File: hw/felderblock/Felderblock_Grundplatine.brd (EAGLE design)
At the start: 100 x 80 mm, 47 parts, among them IC1 LM311N, IC2 LM2936Z-5.0, J1 RJ11, J2 RJ11, M1 ARDUINO-NANO-3.0, T1 BC337, X1 TASTENSPERRE1, X2 TASTENSPERRE2, X3 SCHLUESSELSPERRE, X4 I2C

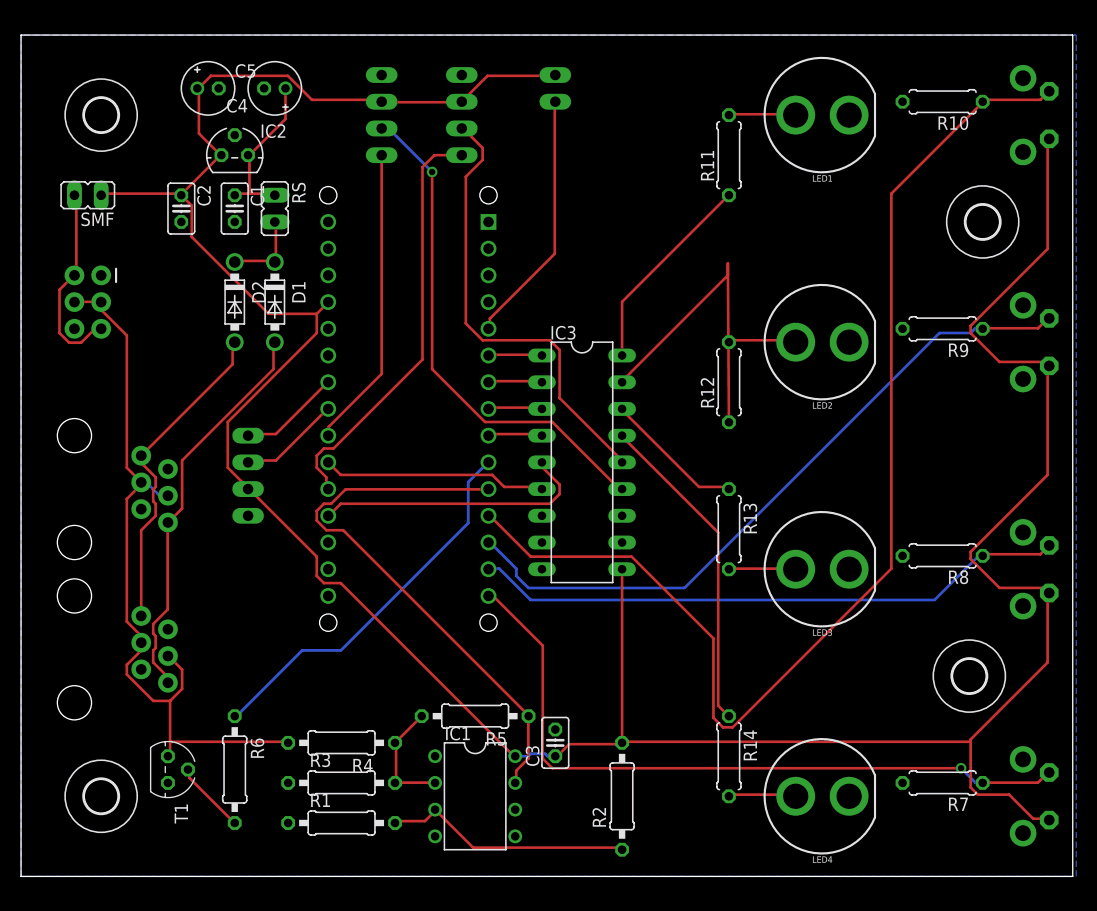
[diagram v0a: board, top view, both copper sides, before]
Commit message: MI+AsT integrated
LED nach I2C, MI links und rechts, AsT und AsM integriert. Board rerouted
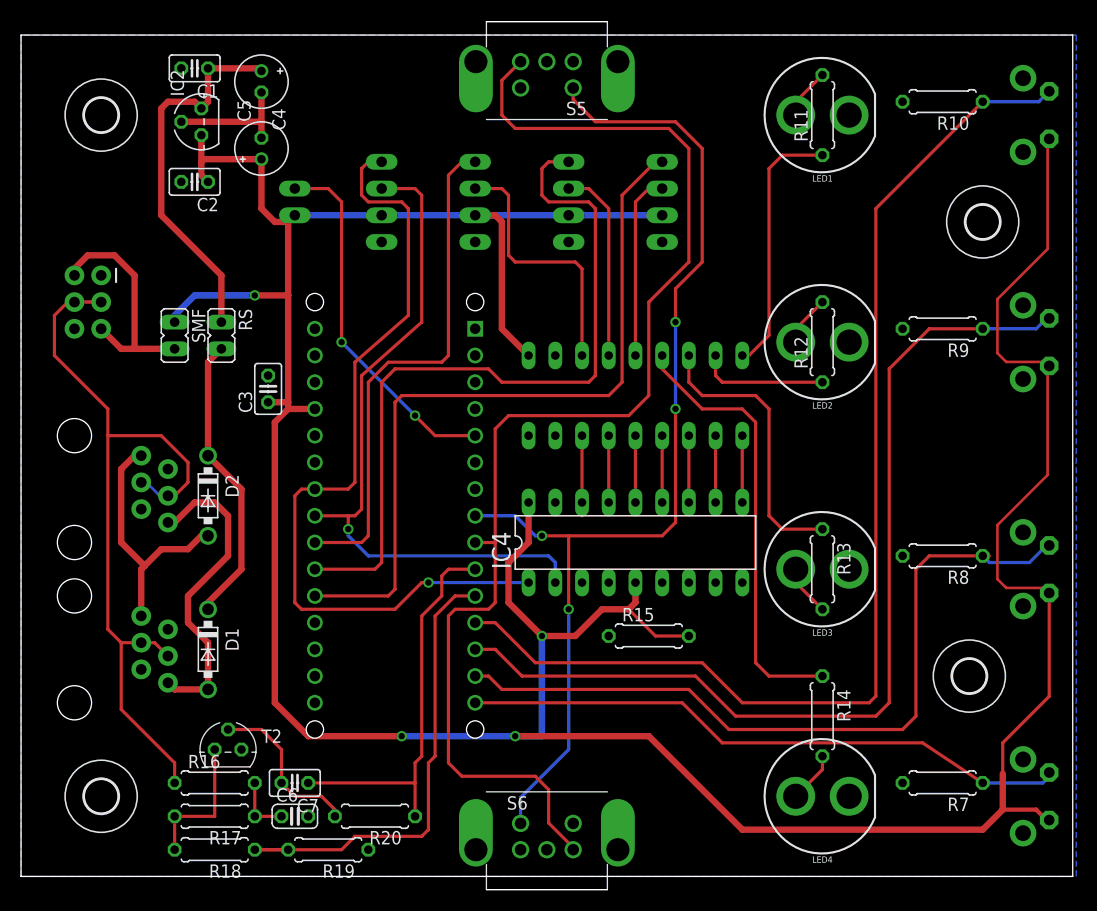
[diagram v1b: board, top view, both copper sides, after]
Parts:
- removed IC1: LM311N, linear:DIL08
- removed R1: 22k, resistor:0207/10
- removed R2: 10k, resistor:0207/10
- removed R3: 150k, resistor:0207/10
- removed R4: 47k, resistor:0207/10
- removed R5: 220k, resistor:0207/10
- removed R6: 2.2k, resistor:0207/10
- removed T1: BC337, transistor:TO92
- added C6: 47pF, resistor:C025-024X044
- added C7: 1nF, resistor:C025-025X050
- added IC4: MCP2300X/P, adafruit:DIL18
- added R15: 1k, resistor:0207/7
- added R16, R17: 12R, resistor:0207/7
- added R18: 130K, resistor:0207/7
- added R19: 47k, resistor:0207/7
- added R20: 3K3, resistor:0207/7
- added S5, S6: EC11B42AE, alps:EC11B42
- added T2: BC337, transistor:TO92
- added X5: ANSCHALTER, con-molex:22-23-2041
- moved C3 43.3 mm to (23.5, 46.4)
- moved D1 33.6 mm to (17.8, 21.6)
- moved X4 29.0 mm to (34.3, 64.1)
- moved X3 27.0 mm to (26.0, 64.1), turned to 90 degrees
- moved X1 20.8 mm to (61.0, 64.1), turned to 90 degrees
- moved X2 19.6 mm to (52.1, 64.1), turned to 90 degrees
- moved D2 18.6 mm to (17.8, 36.2)
- moved SMF 15.7 mm to (14.6, 51.4), turned to 180 degrees
- moved C1 13.9 mm to (16.5, 76.8), turned to 180 degrees
- moved RS 13.1 mm to (19.1, 51.4)
- moved M1 10.2 mm to (35.6, 34.3)
- moved R11 9.67 mm to (76.2, 72.4)
- moved R13 9.67 mm to (76.2, 29.2)
- moved R14 9.67 mm to (76.2, 15.2)
- moved R12 9.67 mm to (76.2, 50.8)
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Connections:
- removed net GND.2: M1.J2.2
- removed net N$1: IC1.3, R1.2, R2.1
- removed net N$18: IC3.7
- removed net N$2: R6.2, T1.2
- removed net N$26: IC3.12
- removed net N$3: IC1.2, R3.2, R4.1, R5.2
- new net AS_LED: IC3.7, IC4.16
- new net AS_LEDD: IC3.12, X5.3
- new net AS_SW: M1.J2.9, X5.4
- new net BASE: C7.2, R20.2, T2.2
- new net LN_INTERN: R17.2, R18.2, T2.3
- new net MI_FWD: M1.J1.9, S5.B, S6.B
- new net MI_SW: M1.J1.8, S5.D, S6.D
- new net N$11: C6.1, R16.2, R17.1
- net +5V: now also IC4.18, IC4.5, R15.2, X5.2; no longer IC1.8, R2.2
- net FELD1_LED: now also IC4.10; no longer M1.J1.6
- net FELD2_LED: now also IC4.11; no longer M1.J1.7
- net FELD3_LED: now also IC4.12; no longer M1.J1.8
- net FELD4_LED: now also IC4.13; no longer M1.J1.9
- net GND: now also C6.2, IC4.3, IC4.4, IC4.6, IC4.8, IC4.9, M1.J2.2, R15.1, R19.1, S5.C, S5.E, S5.GND1, S5.GND2, S6.C, S6.E, S6.GND1, S6.GND2, T2.1, X5.1; no longer IC1.1, IC1.4, R1.1, R3.1, T1.1
- net LN_RX: now also R18.1, R19.2; no longer IC1.7, R5.1
- net LN_TX: now also C7.1, R20.1; no longer R6.1
- net LOCONET: now also R16.1; no longer R4.2, T1.3
- net SCL: now also IC4.1
- net SDA: now also IC4.2
- net TSP1_LED: now also IC4.14; no longer M1.J2.12
- net TSP2_LED: now also IC4.15; no longer M1.J2.10
- net TSP2_SW: now also M1.J2.10; no longer M1.J2.9
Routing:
- net MI_FWD: track 0.00 -> 120.5 mm
- net MI_SW: track 0.00 -> 101.5 mm, vias 0 -> 4
- net SCL: track 9.72 -> 78.0 mm, vias 0 -> 1
- net SDA: track 9.73 -> 65.7 mm, vias 0 -> 1
- net +5V: track 287.5 -> 337.2 mm, vias 0 -> 4
- net AS_SW: track 0.00 -> 48.8 mm
- net TSP2_SW: track 28.8 -> 72.2 mm
- net TSP1_SW: track 40.0 -> 70.9 mm
- net TSP2_LEDD: track 48.2 -> 18.6 mm, vias 1 -> 0
- net TSP1_LEDD: track 43.2 -> 17.7 mm
- net FELD2_SW: track 66.2 -> 91.5 mm
- net AS_LEDD: track 0.00 -> 24.9 mm
- net N$1: track 23.9 -> 0.00 mm
- net N$7: track 15.6 -> 36.3 mm
- net TSP1_LED: track 26.6 -> 6.35 mm
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
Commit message: Update Felderblock_Grundplatine.brd
Mirror MI
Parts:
- flipped S5 to the bottom
- flipped S6 to the bottom
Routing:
- net MI_SW: track 101.5 -> 104.8 mm
- net N$10: vias 0 -> 2
- net LOCONET: vias 0 -> 3
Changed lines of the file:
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@@
 <attribute name="OC_FARNELL" value="1462920" x="34.29" y="64.135" size="1.778" layer="28" rot="MR90" display="off"/>
 </element>
-<element name="S5" library="alps" package="EC11B42" value="EC11B42AE" x="50" y="77.47" rot="R180"/>
-<element name="S6" library="alps" package="EC11B42" value="EC11B42AE" x="50" y="2.54"/>
+<element name="S5" library="alps" package="EC11B42" value="EC11B42AE" x="50" y="77.47" rot="MR180"/>
+<element name="S6" library="alps" package="EC11B42" value="EC11B42AE" x="50" y="2.54" rot="MR0"/>
 <element name="IC4" library="adafruit" package="DIL18" value="MCP2300X/P" x="58.42" y="31.75"/>
 <element name="R15" library="resistor" package="0207/7" value="1k" x="59.69" y="22.86"/>
@@
 <wire x1="9.525" y1="15.875" x2="14.605" y2="10.795" width="0.3048" layer="1"/>
 <wire x1="14.605" y1="10.795" x2="14.605" y2="8.89" width="0.3048" layer="1"/>
+<via x="5.2578" y="54.6354" extent="1-16" drill="0.6" shape="square"/>
+<via x="7.5438" y="54.6354" extent="1-16" drill="0.6" shape="square"/>
+<via x="4.445" y="54.61" extent="1-16" drill="0.6" shape="square"/>
 </signal>
 <signal name="LN_RX">
@@
 <wire x1="8.89" y1="59.055" x2="10.795" y2="57.15" width="0.6096" layer="1"/>
 <wire x1="10.795" y1="57.15" x2="10.795" y2="50.165" width="0.6096" layer="1"/>
+<via x="9.525" y="50.165" extent="1-16" drill="0.6" shape="square"/>
+<via x="5.08" y="57.785" extent="1-16" drill="0.6" shape="square"/>
 </signal>
 <signal name="TSP1_SW">
@@
 <contactref element="S6" pad="B"/>
 <contactref element="M1" pad="J1.9"/>
-<wire x1="52.5" y1="2.54" x2="52.5" y2="2.745" width="0.3048" layer="1"/>
-<wire x1="52.5" y1="2.745" x2="50.165" y2="5.08" width="0.3048" layer="1"/>
-<wire x1="50.165" y1="5.08" x2="50.165" y2="8.255" width="0.3048" layer="1"/>
-<wire x1="50.165" y1="8.255" x2="48.895" y2="9.525" width="0.3048" layer="1"/>
-<wire x1="48.895" y1="9.525" x2="41.91" y2="9.525" width="0.3048" layer="1"/>
 <wire x1="41.91" y1="9.525" x2="40.64" y2="10.795" width="0.3048" layer="1"/>
 <wire x1="40.64" y1="10.795" x2="40.64" y2="24.765" width="0.3048" layer="1"/>
@@
 <wire x1="63.5" y1="58.42" x2="63.5" y2="69.215" width="0.3048" layer="1"/>
 <wire x1="63.5" y1="69.215" x2="61.595" y2="71.12" width="0.3048" layer="1"/>
-<wire x1="61.595" y1="71.12" x2="46.99" y2="71.12" width="0.3048" layer="1"/>
-<wire x1="46.99" y1="71.12" x2="45.72" y2="72.39" width="0.3048" layer="1"/>
-<wire x1="45.72" y1="72.39" x2="45.72" y2="75.69" width="0.3048" layer="1"/>
-<wire x1="45.72" y1="75.69" x2="47.5" y2="77.47" width="0.3048" layer="1"/>
 <wire x1="43.18" y1="31.75" x2="45.085" y2="31.75" width="0.3048" layer="1"/>
+<wire x1="52.5" y1="77.47" x2="52.07" y2="77.47" width="0.254" layer="1"/>
+<wire x1="52.07" y1="77.47" x2="50.8" y2="76.2" width="0.254" layer="1"/>
+<wire x1="50.8" y1="76.2" x2="46.355" y2="76.2" width="0.254" layer="1"/>
+<wire x1="46.355" y1="76.2" x2="45.72" y2="75.565" width="0.254" layer="1"/>
+<wire x1="45.72" y1="75.565" x2="45.72" y2="72.39" width="0.254" layer="1"/>
+<wire x1="45.72" y1="72.39" x2="46.99" y2="71.12" width="0.254" layer="1"/>
+<wire x1="46.99" y1="71.12" x2="61.595" y2="71.12" width="0.254" layer="1"/>
+<wire x1="41.91" y1="9.525" x2="43.18" y2="9.525" width="0.3048" layer="1"/>
+<wire x1="43.18" y1="9.525" x2="45.72" y2="6.985" width="0.3048" layer="1"/>
+<wire x1="45.72" y1="6.985" x2="45.72" y2="3.175" width="0.3048" layer="1"/>
+<wire x1="45.72" y1="3.175" x2="46.355" y2="2.54" width="0.3048" layer="1"/>
+<wire x1="46.355" y1="2.54" x2="47.5" y2="2.54" width="0.3048" layer="1"/>
 </signal>
 <signal name="AS_LED">
@@
 <contactref element="S6" pad="D"/>
 <contactref element="S5" pad="D"/>
-<wire x1="52.5" y1="74.97" x2="52.5" y2="73.865" width="0.3048" layer="1"/>
-<wire x1="52.5" y1="73.865" x2="54.61" y2="71.755" width="0.3048" layer="1"/>
 <wire x1="54.61" y1="71.755" x2="62.23" y2="71.755" width="0.3048" layer="1"/>
 <wire x1="62.23" y1="71.755" x2="64.77" y2="69.215" width="0.3048" layer="1"/>
@@
 <wire x1="48.895" y1="32.385" x2="46.99" y2="34.29" width="0.3048" layer="16"/>
 <wire x1="46.99" y1="34.29" x2="43.18" y2="34.29" width="0.3048" layer="16"/>
-<wire x1="47.5" y1="5.04" x2="47.5" y2="7.495" width="0.3048" layer="16"/>
-<wire x1="47.5" y1="7.495" x2="52.07" y2="12.065" width="0.3048" layer="16"/>
-<wire x1="52.07" y1="12.065" x2="52.07" y2="25.4" width="0.3048" layer="16"/>
+<wire x1="52.07" y1="5.47" x2="52.07" y2="25.4" width="0.3048" layer="16"/>
 <via x="52.07" y="25.4" extent="1-16" drill="0.6" shape="square"/>
 <wire x1="52.07" y1="25.4" x2="52.07" y2="32.385" width="0.3048" layer="1"/>
+<wire x1="54.61" y1="71.755" x2="49.53" y2="71.755" width="0.254" layer="1"/>
+<wire x1="49.53" y1="71.755" x2="47.625" y2="73.66" width="0.254" layer="1"/>
+<wire x1="47.625" y1="73.66" x2="47.625" y2="74.845" width="0.254" layer="1"/>
+<wire x1="47.625" y1="74.845" x2="47.5" y2="74.97" width="0.254" layer="1"/>
+<wire x1="52.07" y1="5.47" x2="52.5" y2="5.04" width="0.3048" layer="16"/>
 </signal>
 <signal name="TSP2_SW">

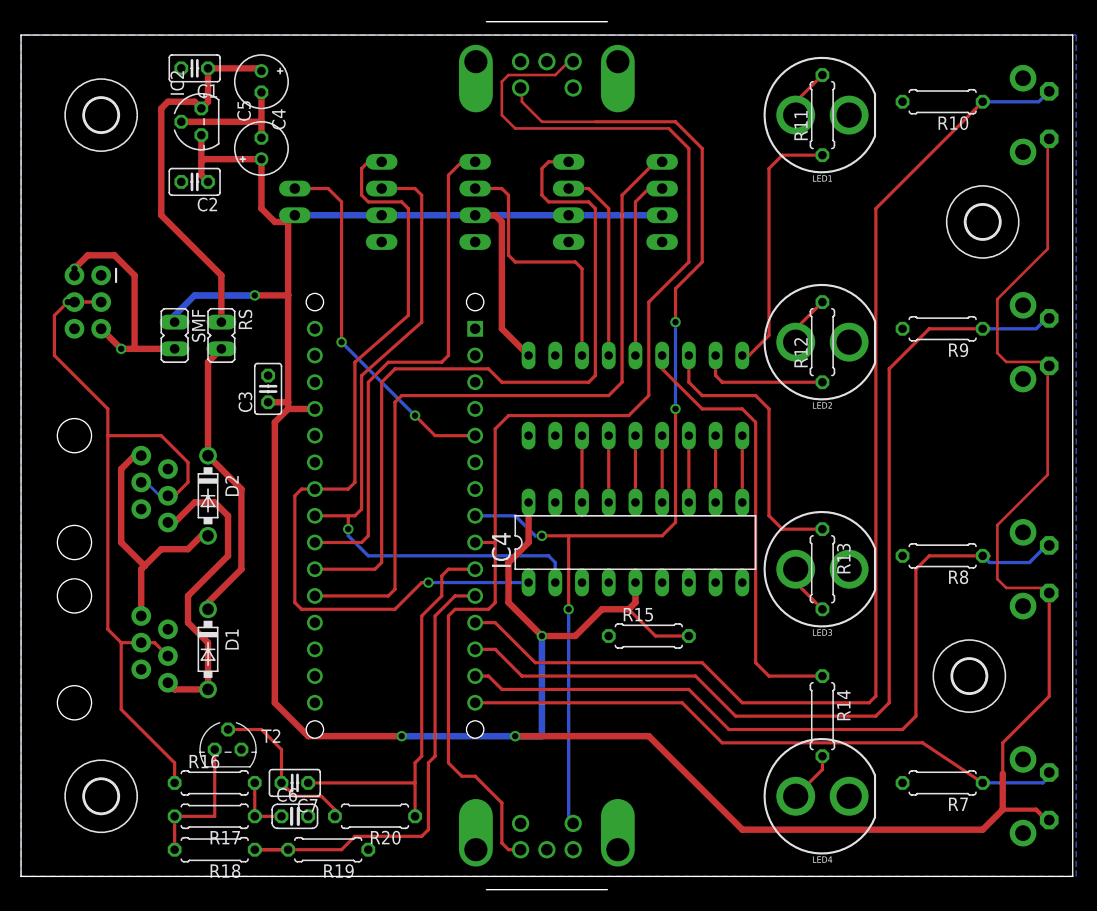
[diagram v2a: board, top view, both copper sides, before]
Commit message: Changed pin order on MCP
MCP moved to other side, changed pin order
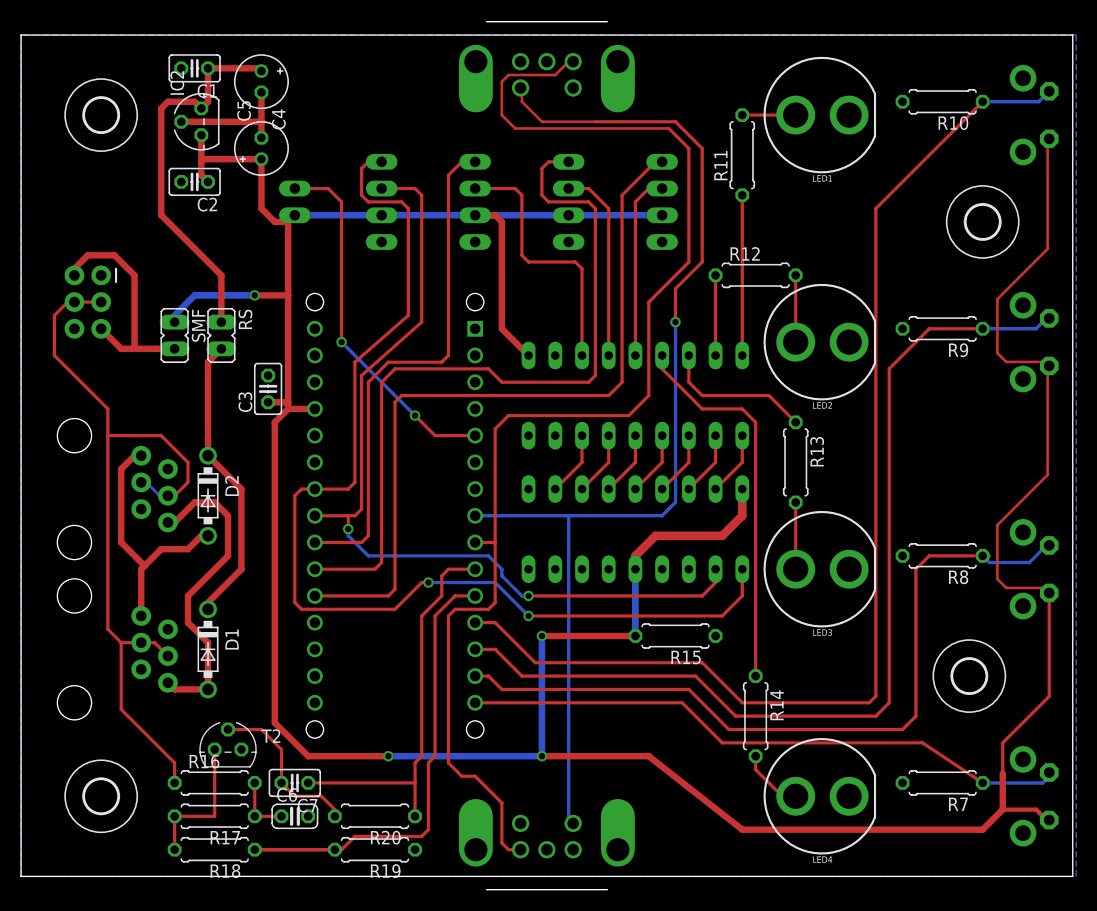
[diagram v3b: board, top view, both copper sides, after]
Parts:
- IC3: value (none) -> ULN2803
- moved R13 10.5 mm to (73.7, 39.4)
- moved R12 8.98 mm to (69.8, 57.1), turned to 0 degrees
- moved R11 8.52 mm to (68.6, 68.6)
- moved R14 6.35 mm to (69.8, 15.2)
- moved R19 4.45 mm to (33.7, 2.54)
- moved R15 2.54 mm to (62.2, 22.9), turned to 180 degrees
- moved IC4 1.27 mm to (58.4, 33.0), flipped to the bottom
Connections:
- net AS_LED: now also IC4.11; no longer IC4.16
- net FELD1_LED: now also IC4.17; no longer IC4.10
- net FELD2_LED: now also IC4.16; no longer IC4.11
- net FELD3_LED: now also IC4.15; no longer IC4.12
- net FELD4_LED: now also IC4.14; no longer IC4.13
- net TSP1_LED: now also IC4.13; no longer IC4.14
- net TSP2_LED: now also IC4.12; no longer IC4.15
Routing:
- net SCL: track 78.0 -> 102.9 mm, vias 1 -> 2
- net SDA: track 65.7 -> 82.6 mm, vias 1 -> 2
- net FELD3_LEDD: track 27.0 -> 14.3 mm
- net FELD1_LEDD: track 24.8 -> 15.2 mm
- net FELD4_LEDD: track 42.0 -> 36.4 mm
- net FELD2_LEDD: track 12.3 -> 7.62 mm
- net LN_RX: track 45.7 -> 50.1 mm
- net +5V: track 337.2 -> 334.3 mm
- net N$8: track 4.86 -> 7.62 mm
- net LOCONET: track 77.9 -> 75.4 mm, vias 3 -> 0
- net N$5: track 4.86 -> 6.35 mm
- net AS_LED: track 7.62 -> 6.13 mm
- net N$9: track 4.86 -> 6.13 mm
- net MI_SW: track 104.8 -> 104.1 mm, vias 4 -> 1
- net N$10: vias 2 -> 0

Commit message: housekeeping
some reroutes, text optimized
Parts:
- IC2: value LM2936Z-5.0 -> LM2936
- moved S5 2.10 mm to (52.0, 76.8)
- moved S6 2.10 mm to (52.0, 3.17)
- flipped RS to the bottom
- flipped SMF to the bottom
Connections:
- net MI_FWD: now also S5.A, S6.A
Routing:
- net MI_SW: track 104.1 -> 120.6 mm, vias 1 -> 2
- net +5V: track 334.3 -> 325.9 mm
- net MI_FWD: track 120.7 -> 124.3 mm, vias 0 -> 2
- net N$8: track 7.62 -> 6.35 mm
- net TSP2_SW: track 72.2 -> 71.3 mm
